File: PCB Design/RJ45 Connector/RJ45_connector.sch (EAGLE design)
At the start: 3 parts, among them X1 RJ45-8L-B

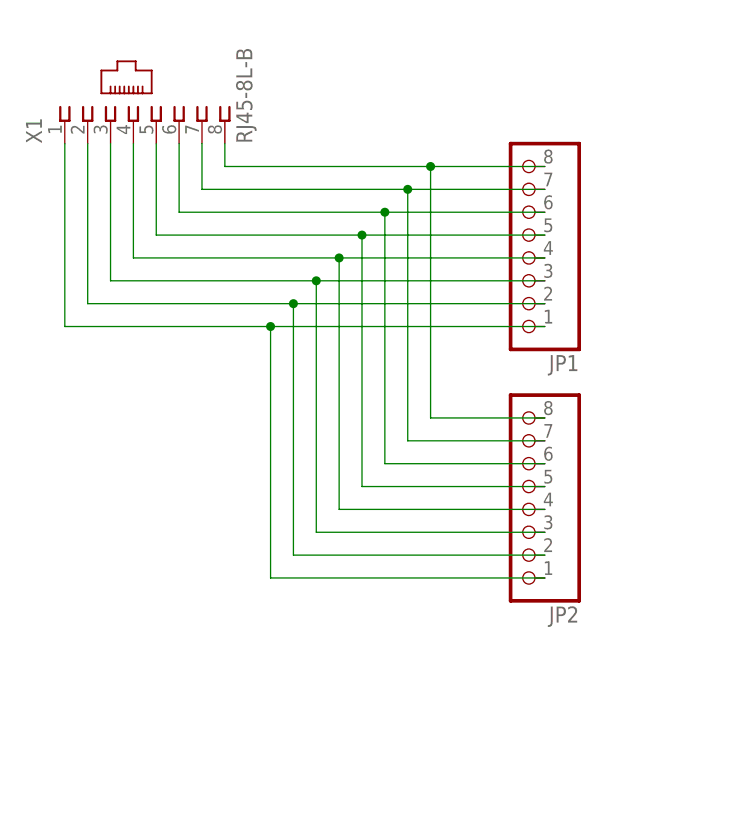
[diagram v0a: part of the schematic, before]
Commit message: Routed the RJ45 connector with side and top headers
Also added the accelerometer chip to the library
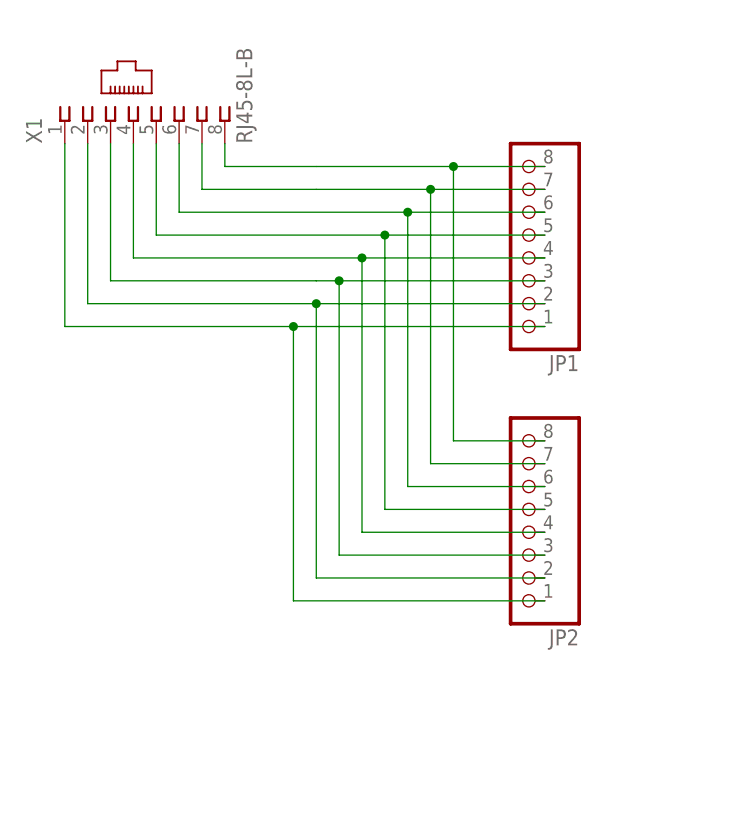
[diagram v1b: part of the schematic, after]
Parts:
- JP1, JP2: device pinhead:PINHD-1X8 -> CBLA_Test_bed_Library:PINHD-1X8/90
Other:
- moved on the sheet: JP2

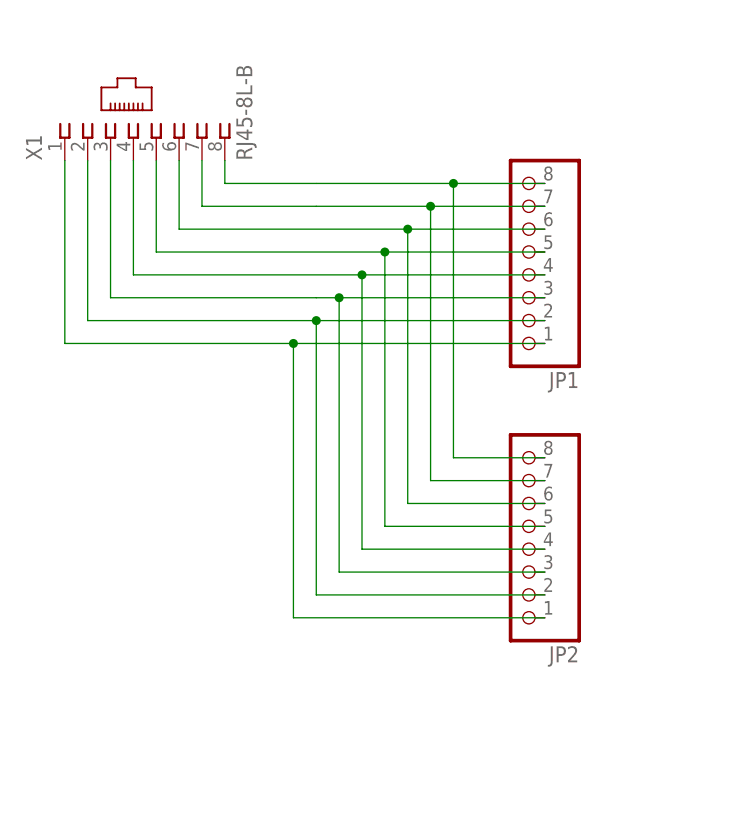
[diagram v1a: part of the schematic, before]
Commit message: Changed location of the header to make it much easier to router
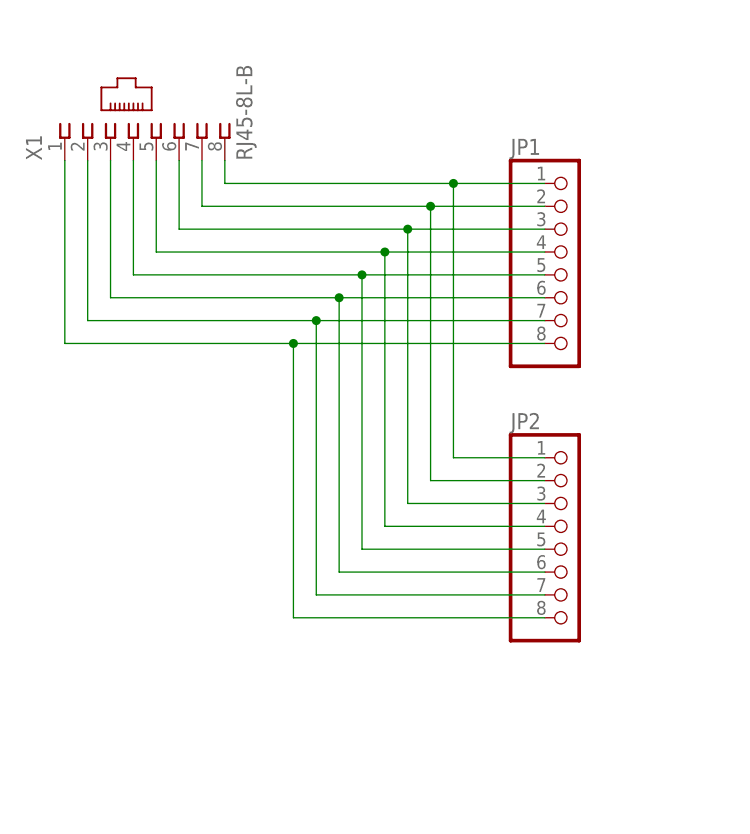
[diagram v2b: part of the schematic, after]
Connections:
- net N$1: now also JP1.1, JP2.1; no longer JP1.8, JP2.8
- net N$2: now also JP1.2, JP2.2; no longer JP1.7, JP2.7
- net N$3: now also JP1.3, JP2.3; no longer JP1.6, JP2.6
- net N$4: now also JP1.4, JP2.4; no longer JP1.5, JP2.5
- net N$5: now also JP1.5, JP2.5; no longer JP1.4, JP2.4
- net N$6: now also JP1.6, JP2.6; no longer JP1.3, JP2.3
- net N$7: now also JP1.7, JP2.7; no longer JP1.2, JP2.2
- net N$8: now also JP1.8, JP2.8; no longer JP1.1, JP2.1
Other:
- moved on the sheet: JP1, JP2
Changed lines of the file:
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@@
 </classes>
 <parts>
+<part name="X1" library="CBLA_Test_bed_Library" deviceset="RJ45" device="" technology="-8L-B"/>
 <part name="JP1" library="CBLA_Test_bed_Library" deviceset="PINHD-1X8" device="/90"/>
-<part name="X1" library="CBLA_Test_bed_Library" deviceset="RJ45" device="" technology="-8L-B"/>
 <part name="JP2" library="CBLA_Test_bed_Library" deviceset="PINHD-1X8" device="/90"/>
 </parts>
@@
 </plain>
 <instances>
-<instance part="JP1" gate="A" x="185.42" y="104.14" rot="R180"/>
 <instance part="X1" gate="G$1" x="142.24" y="116.84" rot="R90"/>
-<instance part="JP2" gate="A" x="185.42" y="73.66" rot="R180"/>
+<instance part="JP1" gate="A" x="190.5" y="101.6"/>
+<instance part="JP2" gate="A" x="190.5" y="71.12"/>
 </instances>
 <busses>
@@
 <pinref part="X1" gate="G$1" pin="8"/>
 <wire x1="152.4" y1="114.3" x2="152.4" y2="111.76" width="0.1524" layer="91"/>
-<wire x1="162.56" y1="111.76" x2="177.8" y2="111.76" width="0.1524" layer="91"/>
-<pinref part="JP1" gate="A" pin="8"/>
+<wire x1="152.4" y1="111.76" x2="177.8" y2="111.76" width="0.1524" layer="91"/>
 <wire x1="177.8" y1="111.76" x2="187.96" y2="111.76" width="0.1524" layer="91"/>
-<wire x1="152.4" y1="111.76" x2="162.56" y2="111.76" width="0.1524" layer="91"/>
-<pinref part="JP2" gate="A" pin="8"/>
 <wire x1="177.8" y1="81.28" x2="187.96" y2="81.28" width="0.1524" layer="91"/>
 <wire x1="177.8" y1="111.76" x2="177.8" y2="81.28" width="0.1524" layer="91"/>
 <junction x="177.8" y="111.76"/>
+<pinref part="JP1" gate="A" pin="1"/>
+<pinref part="JP2" gate="A" pin="1"/>
 </segment>
 </net>
@@
 <segment>
 <pinref part="X1" gate="G$1" pin="7"/>
-<pinref part="JP1" gate="A" pin="7"/>
 <wire x1="149.86" y1="114.3" x2="149.86" y2="109.22" width="0.1524" layer="91"/>
-<wire x1="162.56" y1="109.22" x2="175.26" y2="109.22" width="0.1524" layer="91"/>
 <wire x1="175.26" y1="109.22" x2="187.96" y2="109.22" width="0.1524" layer="91"/>
-<wire x1="149.86" y1="109.22" x2="162.56" y2="109.22" width="0.1524" layer="91"/>
-<pinref part="JP2" gate="A" pin="7"/>
+<wire x1="149.86" y1="109.22" x2="175.26" y2="109.22" width="0.1524" layer="91"/>
 <wire x1="175.26" y1="78.74" x2="187.96" y2="78.74" width="0.1524" layer="91"/>
 <wire x1="175.26" y1="109.22" x2="175.26" y2="78.74" width="0.1524" layer="91"/>
 <junction x="175.26" y="109.22"/>
+<pinref part="JP1" gate="A" pin="2"/>
+<pinref part="JP2" gate="A" pin="2"/>
 </segment>
 </net>
 <net name="N$3" class="0">
 <segment>
-<pinref part="JP1" gate="A" pin="6"/>
 <wire x1="172.72" y1="106.68" x2="187.96" y2="106.68" width="0.1524" layer="91"/>
 <wire x1="147.32" y1="106.68" x2="172.72" y2="106.68" width="0.1524" layer="91"/>
-<pinref part="JP2" gate="A" pin="6"/>
 <wire x1="172.72" y1="76.2" x2="187.96" y2="76.2" width="0.1524" layer="91"/>
 <wire x1="172.72" y1="106.68" x2="172.72" y2="76.2" width="0.1524" layer="91"/>
@@
 <pinref part="X1" gate="G$1" pin="6"/>
 <wire x1="147.32" y1="114.3" x2="147.32" y2="106.68" width="0.1524" layer="91"/>
+<pinref part="JP1" gate="A" pin="3"/>
+<pinref part="JP2" gate="A" pin="3"/>
 </segment>
 </net>
@@
 <segment>
 <pinref part="X1" gate="G$1" pin="5"/>
-<pinref part="JP1" gate="A" pin="5"/>
 <wire x1="144.78" y1="114.3" x2="144.78" y2="104.14" width="0.1524" layer="91"/>
 <wire x1="144.78" y1="104.14" x2="170.18" y2="104.14" width="0.1524" layer="91"/>
 <wire x1="170.18" y1="104.14" x2="187.96" y2="104.14" width="0.1524" layer="91"/>
-<pinref part="JP2" gate="A" pin="5"/>
 <wire x1="170.18" y1="73.66" x2="187.96" y2="73.66" width="0.1524" layer="91"/>
 <wire x1="170.18" y1="104.14" x2="170.18" y2="73.66" width="0.1524" layer="91"/>
 <junction x="170.18" y="104.14"/>
+<pinref part="JP1" gate="A" pin="4"/>
+<pinref part="JP2" gate="A" pin="4"/>
 </segment>
 </net>
@@
 <pinref part="X1" gate="G$1" pin="4"/>
 <wire x1="142.24" y1="114.3" x2="142.24" y2="101.6" width="0.1524" layer="91"/>
-<pinref part="JP1" gate="A" pin="4"/>
 <wire x1="142.24" y1="101.6" x2="167.64" y2="101.6" width="0.1524" layer="91"/>
 <wire x1="167.64" y1="101.6" x2="187.96" y2="101.6" width="0.1524" layer="91"/>
-<pinref part="JP2" gate="A" pin="4"/>
 <wire x1="167.64" y1="71.12" x2="187.96" y2="71.12" width="0.1524" layer="91"/>
 <wire x1="167.64" y1="101.6" x2="167.64" y2="71.12" width="0.1524" layer="91"/>
 <junction x="167.64" y="101.6"/>
+<pinref part="JP1" gate="A" pin="5"/>
+<pinref part="JP2" gate="A" pin="5"/>
 </segment>
 </net>
@@
 <segment>
 <pinref part="X1" gate="G$1" pin="3"/>
-<pinref part="JP1" gate="A" pin="3"/>
 <wire x1="139.7" y1="114.3" x2="139.7" y2="99.06" width="0.1524" layer="91"/>
-<wire x1="162.56" y1="99.06" x2="165.1" y2="99.06" width="0.1524" layer="91"/>
 <wire x1="165.1" y1="99.06" x2="187.96" y2="99.06" width="0.1524" layer="91"/>
-<wire x1="139.7" y1="99.06" x2="162.56" y2="99.06" width="0.1524" layer="91"/>
-<pinref part="JP2" gate="A" pin="3"/>
+<wire x1="139.7" y1="99.06" x2="165.1" y2="99.06" width="0.1524" layer="91"/>
 <wire x1="165.1" y1="68.58" x2="187.96" y2="68.58" width="0.1524" layer="91"/>
 <wire x1="165.1" y1="99.06" x2="165.1" y2="68.58" width="0.1524" layer="91"/>
 <junction x="165.1" y="99.06"/>
+<pinref part="JP1" gate="A" pin="6"/>
+<pinref part="JP2" gate="A" pin="6"/>
 </segment>
 </net>
 <net name="N$7" class="0">
 <segment>
-<pinref part="JP1" gate="A" pin="2"/>
 <pinref part="X1" gate="G$1" pin="2"/>
 <wire x1="187.96" y1="96.52" x2="162.56" y2="96.52" width="0.1524" layer="91"/>
 <wire x1="137.16" y1="96.52" x2="137.16" y2="114.3" width="0.1524" layer="91"/>
 <wire x1="162.56" y1="96.52" x2="137.16" y2="96.52" width="0.1524" layer="91"/>
-<pinref part="JP2" gate="A" pin="2"/>
 <wire x1="187.96" y1="66.04" x2="162.56" y2="66.04" width="0.1524" layer="91"/>
 <wire x1="162.56" y1="96.52" x2="162.56" y2="66.04" width="0.1524" layer="91"/>
 <junction x="162.56" y="96.52"/>
+<pinref part="JP1" gate="A" pin="7"/>
+<pinref part="JP2" gate="A" pin="7"/>
 </segment>
 </net>
 <net name="N$8" class="0">
 <segment>
-<pinref part="JP1" gate="A" pin="1"/>
 <pinref part="X1" gate="G$1" pin="1"/>
 <wire x1="187.96" y1="93.98" x2="160.02" y2="93.98" width="0.1524" layer="91"/>
 <wire x1="134.62" y1="93.98" x2="134.62" y2="114.3" width="0.1524" layer="91"/>
 <wire x1="160.02" y1="93.98" x2="134.62" y2="93.98" width="0.1524" layer="91"/>
-<pinref part="JP2" gate="A" pin="1"/>
 <wire x1="187.96" y1="63.5" x2="160.02" y2="63.5" width="0.1524" layer="91"/>
 <wire x1="160.02" y1="93.98" x2="160.02" y2="63.5" width="0.1524" layer="91"/>
 <junction x="160.02" y="93.98"/>
+<pinref part="JP1" gate="A" pin="8"/>
+<pinref part="JP2" gate="A" pin="8"/>
 </segment>
 </net>
